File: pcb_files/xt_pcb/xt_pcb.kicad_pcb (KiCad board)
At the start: 2 copper layers, 400.1 x 95.2 mm, 193 parts, among them J1 JST, SW1 RST, SW10 SW_Push, SW11 SW_Push, SW12 SW_Push, SW13 SW_Push, SW14 SW_Push, SW15 SW_Push, SW16 SW_Push, SW17 SW_Push, SW18 SW_Push, SW19 SW_Push, SW2 RST, SW20 SW_Push, SW21 SW_Push, SW22 SW_Push, SW23 SW_Push, SW24 SW_Push, SW25 SW_Push, SW26 SW_Push, SW27 SW_Push, SW28 SW_Push, SW29 SW_Push, SW3 SW_Push, SW30 SW_Push, SW31 SW_Push, SW32 SW_Push, SW33 SW_Push, SW34 SW_Push, SW35 SW_Push, SW36 SW_Push, SW37 SW_Push, SW38 SW_Push, SW39 SW_Push, SW4 SW_Push, SW40 SW_Push, SW41 SW_Push, SW42 SW_Push, SW43 SW_Push, SW44 SW_Push, SW45 SW_Push, SW46 SW_Push, SW47 SW_Push, SW48 SW_Push, SW49 SW_Push, SW5 SW_Push, SW50 SW_Push, SW51 SW_Push, SW52 SW_Push, SW53 SW_Push, SW54 SW_Push, SW55 SW_Push, SW56 SW_Push, SW57 SW_Push, SW58 SW_Push, SW59 SW_Push, SW6 SW_Push, SW60 SW_Push, SW61 SW_Push, SW62 SW_Push, SW63 SW_Push, SW64 SW_Push, SW65 SW_Push, SW66 SW_Push, SW67 SW_Push, SW68 SW_Push, SW69 SW_Push, SW7 SW_Push, SW70 SW_Push, SW71 SW_Push, SW72 SW_Push, SW73 SW_Push, SW74 SW_Push, SW75 SW_Push, SW76 SW_Push, SW77 SW_Push, SW78 SW_Push, SW79 SW_Push, SW8 SW_Push, SW80 SW_Push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

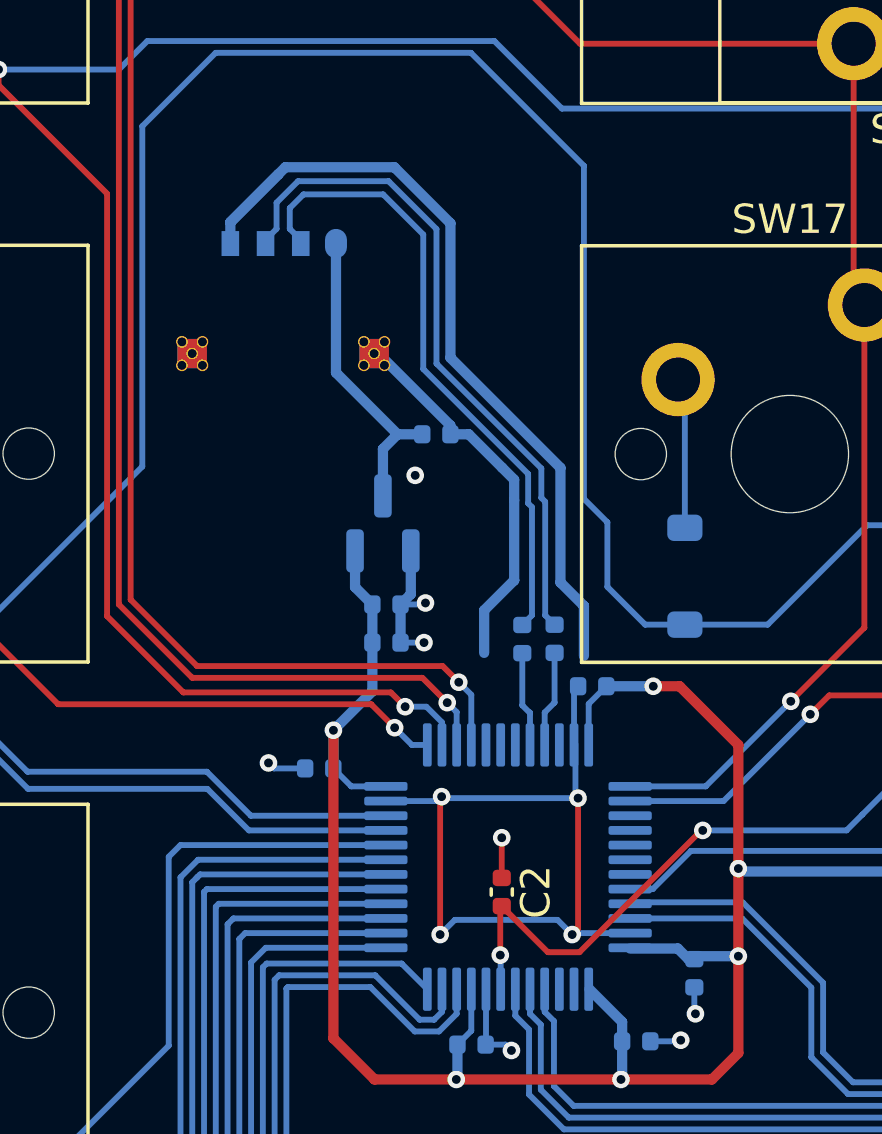
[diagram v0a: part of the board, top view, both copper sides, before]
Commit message: 0603 handsolder
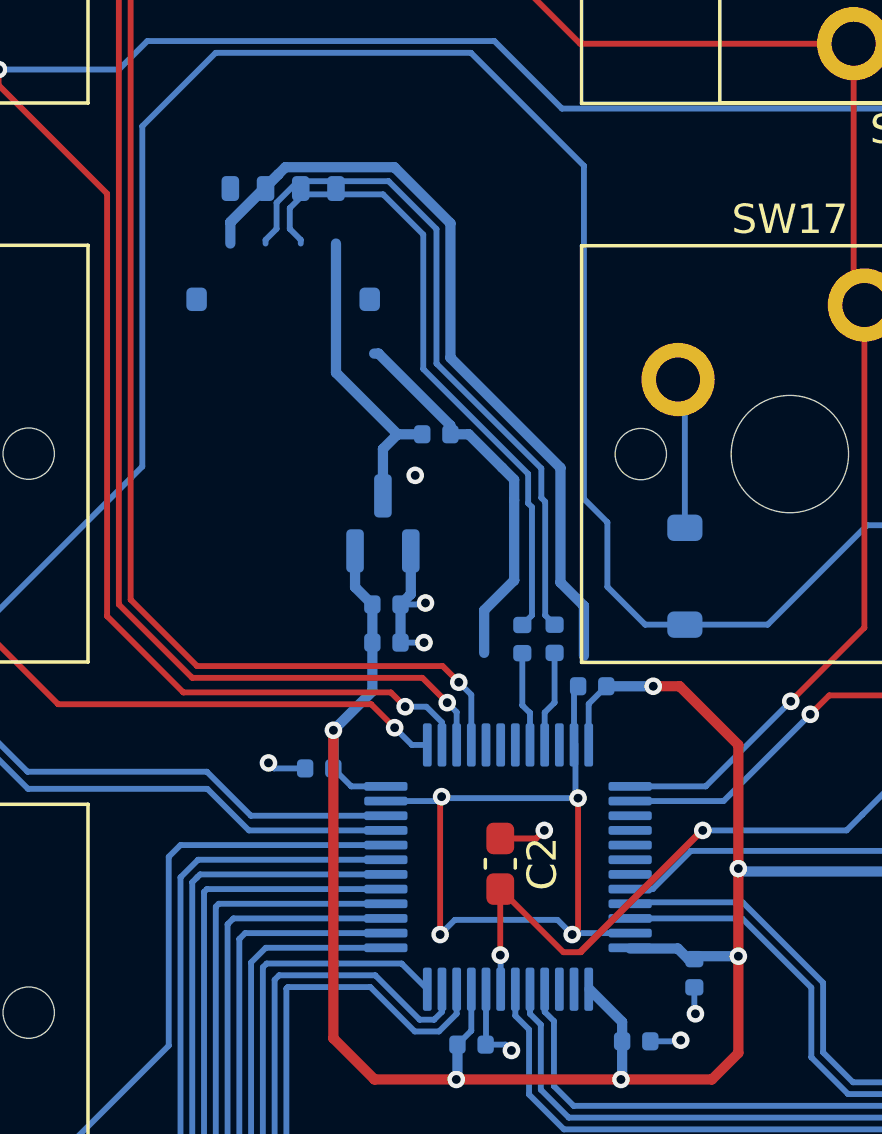
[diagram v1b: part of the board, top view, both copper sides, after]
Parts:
- C2: footprint Capacitor_SMD:C_0402_1005Metric -> Capacitor_SMD:C_0603_1608Metric_Pad1.08x0.95mm_HandSolder
- J1: footprint acheron_Connectors:MOLEX_781710004_MountingReliefs -> Connector_Molex:Molex_Pico-EZmate_78171-0004_1x04-1MP_P1.20mm_Vertical
- SW17: footprint PCM_Switch_Keyboard_Cherry_MX:SW_Cherry_MX_PCB_1.25u -> PCM_Switch_Keyboard_Cherry_MX:SW_Cherry_MX_PCB_2.25u
- SW72: footprint PCM_Switch_Keyboard_Cherry_MX:SW_Cherry_MX_PCB_1.75u -> PCM_Switch_Keyboard_Cherry_MX:SW_Cherry_MX_PCB_2.75u
- moved C2 0.96 mm to (115.7, 161.6)
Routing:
- net Net-(J1-Pin_3): track 23.1 -> 51.9 mm
- net GND: track 90.5 -> 62.0 mm
- net NRST: track 25.9 -> 32.6 mm

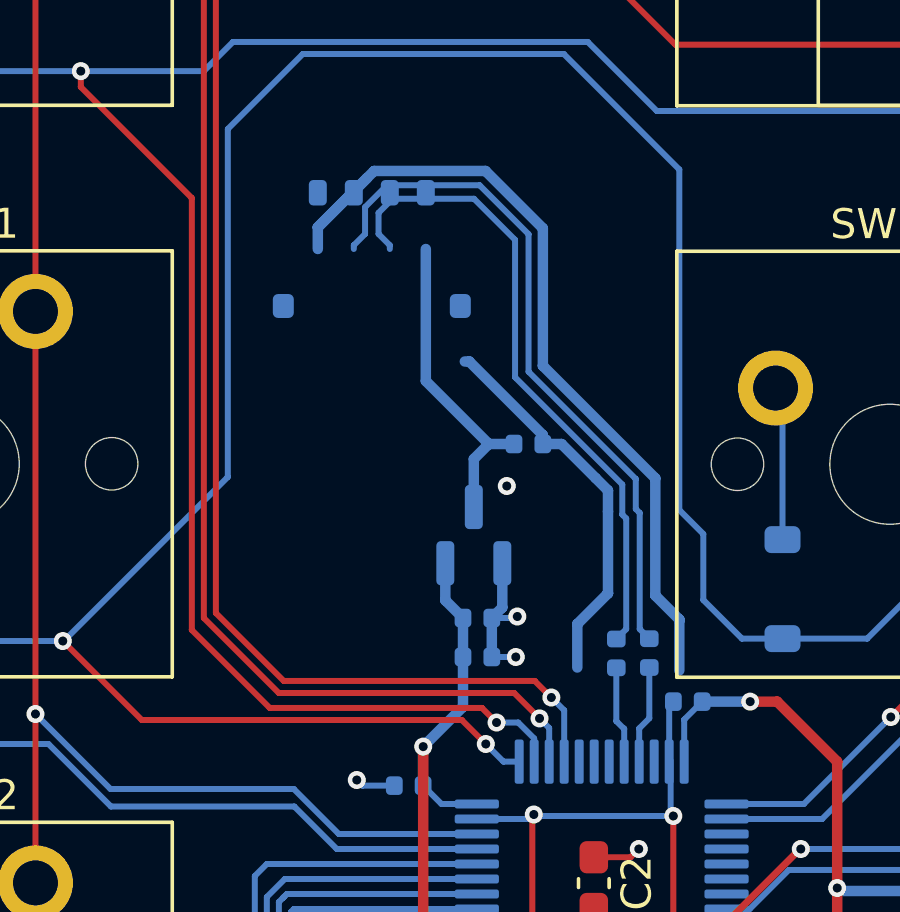
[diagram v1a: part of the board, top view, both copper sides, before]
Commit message: allignment fix
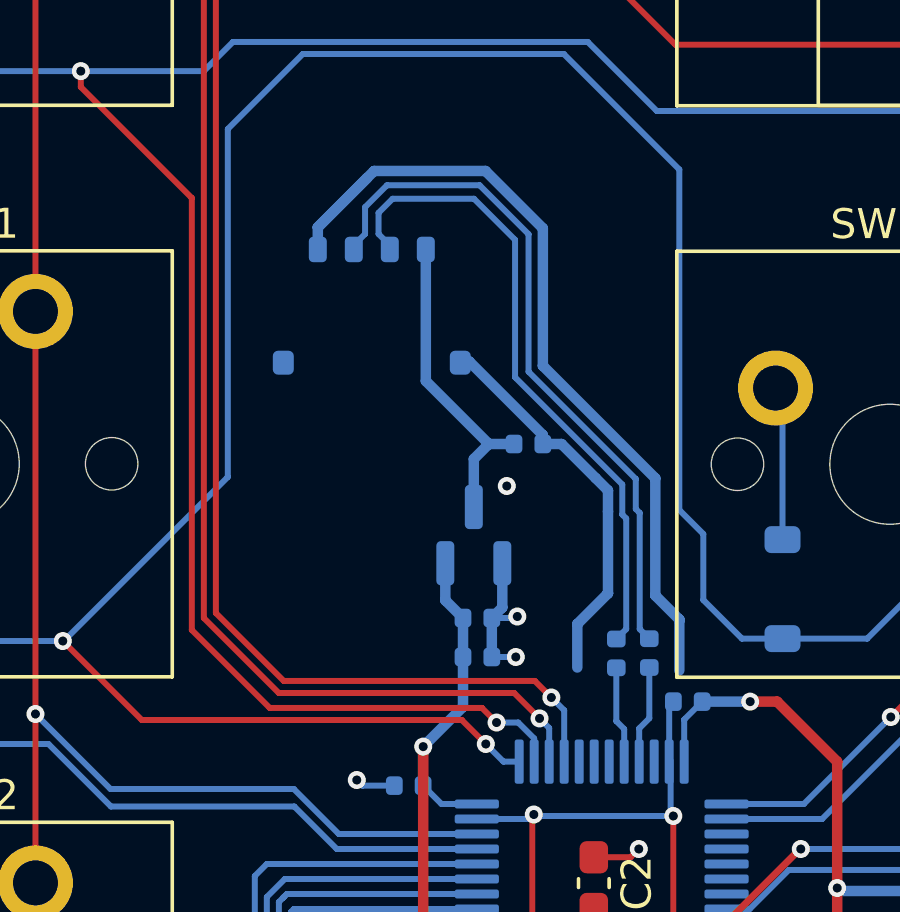
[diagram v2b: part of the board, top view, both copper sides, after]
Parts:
- moved J1 1.89 mm to (108.3, 142.3)
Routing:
- net GND: track 62.0 -> 90.8 mm
- net Net-(J1-Pin_3): track 51.9 -> 23.1 mm
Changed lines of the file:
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@@
 	(footprint "Connector_Molex:Molex_Pico-EZmate_78171-0004_1x04-1MP_P1.20mm_Vertical"
 		(layer "B.Cu")
-		(at 108.2615 140.445 180)
+		(at 108.2615 142.335 180)
 		(descr "Molex Pico-EZmate series connector, 78171-0004 (http://www.molex.com/pdm_docs/sd/781710002_sd.pdf), generated with kicad-footprint-generator")
 		(tags "connector Molex Pico-EZmate vertical")
@@
 	)
 	(segment
-		(start 111.6615 149.045)
-		(end 111.6615 147.445)
+		(start 110.0615 144.845)
+		(end 110.0615 140.46)
 		(width 0.35)
 		(layer "B.Cu")
@@
 	)
 	(segment
-		(start 111.6615 147.445)
-		(end 112.1615 146.945)
+		(start 111.6615 149.045)
+		(end 111.6615 147.445)
 		(width 0.35)
 		(layer "B.Cu")
@@
 	)
 	(segment
-		(start 110.0615 140.445)
-		(end 110.0615 144.845)
+		(start 111.6615 147.445)
+		(end 112.1615 146.945)
 		(width 0.35)
 		(layer "B.Cu")
@@
 	)
 	(segment
+		(start 112.051864 137.844)
+		(end 113.9625 139.754636)
+		(width 0.35)
+		(layer "B.Cu")
+		(net 2)
+	)
+	(segment
 		(start 112.6115 150.92)
 		(end 112.6115 152.395)
@@
 	)
 	(segment
+		(start 106.4615 139.72)
+		(end 108.099 138.0825)
+		(width 0.35)
+		(layer "B.Cu")
+		(net 2)
+	)
+	(segment
+		(start 108.099 138.0825)
+		(end 108.337501 137.844)
+		(width 0.35)
+		(layer "B.Cu")
+		(net 2)
+	)
+	(segment
 		(start 115.174 165.8575)
 		(end 115.174 167.7325)
@@
 	)
 	(segment
+		(start 118.5115 152.795)
+		(end 118.5115 154.495)
+		(width 0.35)
+		(layer "B.Cu")
+		(net 2)
+	)
+	(segment
+		(start 118.5115 152.795)
+		(end 118.5115 152.845)
+		(width 0.35)
+		(layer "B.Cu")
+		(net 2)
+	)
+	(segment
 		(start 113.9615 146.945)
 		(end 114.5865 146.945)
@@
 	)
 	(segment
+		(start 117.7115 148.0873)
+		(end 117.7115 151.995)
+		(width 0.35)
+		(layer "B.Cu")
+		(net 2)
+	)
+	(segment
 		(start 113.6115 163.995)
 		(end 114.1125 163.494)
@@
 	)
 	(segment
+		(start 108.337501 137.844)
+		(end 112.051864 137.844)
+		(width 0.35)
+		(layer "B.Cu")
+		(net 2)
+	)
+	(segment
 		(start 114.1125 163.494)
 		(end 117.6105 163.494)
@@
 	)
 	(segment
+		(start 113.9625 144.3383)
+		(end 117.7115 148.0873)
+		(width 0.35)
+		(layer "B.Cu")
+		(net 2)
+	)
+	(segment
 		(start 122.274 166.6575)
 		(end 122.3115 166.695)
@@
 	)
 	(segment
+		(start 106.4615 139.720001)
+		(end 108.099 138.0825)
+		(width 0.35)
+		(layer "B.Cu")
+		(net 2)
+	)
+	(segment
+		(start 117.7115 151.995)
+		(end 118.5115 152.795)
+		(width 0.35)
+		(layer "B.Cu")
+		(net 2)
+	)
+	(segment
 		(start 113.0615 152.745)
 		(end 113.1115 152.695)
@@
 	)
 	(segment
+		(start 106.4615 140.445)
+		(end 106.4615 139.72)
+		(width 0.35)
+		(layer "B.Cu")
+		(net 2)
+	)
+	(segment
 		(start 112.2615 154.045)
 		(end 113.0615 154.045)
@@
 	)
 	(segment
+		(start 113.9625 139.754636)
+		(end 113.9625 144.3383)
+		(width 0.35)
+		(layer "B.Cu")
+		(net 2)
+	)
+	(segment
 		(start 434.6815 111.795)
 		(end 434.6815 108.0465)
@@
 	)
 	(segment
-		(start 116.674 156.426249)
-		(end 116.674 156.445)
-		(width 0.2)
-		(layer "B.Cu")
-		(net 116)
-	)
-	(segment
 		(start 116.674 156.445)
 		(end 116.4115 156.1825)
@@
 	)
 	(segment
-		(start 112.051864 137.844)
-		(end 113.9625 139.754636)
-		(width 0.35)
-		(layer "B.Cu")
-		(net 129)
-	)
-	(segment
 		(start 108.0365 139.945)
 		(end 107.6615 140.32)
@@
 	)
 	(segment
-		(start 106.4615 139.72)
-		(end 108.099 138.0825)
-		(width 0.35)
-		(layer "B.Cu")
-		(net 129)
-	)
-	(segment
 		(start 108.0365 139.051802)
 		(end 108.0365 139.945)
@@
 	)
 	(segment
-		(start 108.099 138.0825)
-		(end 108.337501 137.844)
-		(width 0.35)
-		(layer "B.Cu")
-		(net 129)
-	)
-	(segment
-		(start 118.5115 152.795)
-		(end 118.5115 154.495)
-		(width 0.35)
-		(layer "B.Cu")
-		(net 129)
-	)
-	(segment
-		(start 118.5115 152.795)
-		(end 118.5115 152.845)
-		(width 0.35)
-		(layer "B.Cu")
-		(net 129)
-	)
-	(segment
 		(start 117.191501 153.115001)
 		(end 117.191501 149.242101)
@@
 	)
 	(segment
-		(start 117.7115 148.0873)
-		(end 117.7115 151.995)
-		(width 0.35)
-		(layer "B.Cu")
-		(net 129)
-	)
-	(segment
-		(start 108.337501 137.844)
-		(end 112.051864 137.844)
-		(width 0.35)
-		(layer "B.Cu")
-		(net 129)
-	)
-	(segment
 		(start 113.4865 139.951802)
 		(end 111.854698 138.32)
@@
 	)
 	(segment
-		(start 113.9625 144.3383)
-		(end 117.7115 148.0873)
-		(width 0.35)
-		(layer "B.Cu")
-		(net 129)
-	)
-	(segment
 		(start 117.0605 148.109466)
 		(end 113.4865 144.535466)
@@
 	)
 	(segment
-		(start 106.4615 139.720001)
-		(end 108.099 138.0825)
-		(width 0.35)
-		(layer "B.Cu")
-		(net 129)
-	)
-	(segment
-		(start 117.7115 151.995)
-		(end 118.5115 152.795)
-		(width 0.35)
-		(layer "B.Cu")
-		(net 129)
-	)
-	(segment
 		(start 108.768302 138.32)
 		(end 108.0365 139.051802)
@@
 		(layer "B.Cu")
 		(net 129)
-	)
-	(segment
-		(start 106.4615 140.445)
-		(end 106.4615 139.72)
-		(width 0.35)
-		(layer "B.Cu")
-		(net 129)
-	)
-	(segment
-		(start 113.9625 139.754636)
-		(end 113.9625 144.3383)
-		(width 0.35)
-		(layer "B.Cu")
-		(net 129)

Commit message: new footprint
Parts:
- SW17: footprint PCM_Switch_Keyboard_Cherry_MX:SW_Cherry_MX_PCB_2.25u -> PCM_Switch_Keyboard_Cherry_MX:SW_Cherry_MX_PCB_1.25u
- SW72: footprint PCM_Switch_Keyboard_Cherry_MX:SW_Cherry_MX_PCB_2.75u -> PCM_Switch_Keyboard_Cherry_MX:SW_Cherry_MX_Plate_1.75u
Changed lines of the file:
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@@
 		)
 	)
-	(footprint "PCM_Switch_Keyboard_Cherry_MX:SW_Cherry_MX_PCB_2.75u"
+	(footprint "PCM_Switch_Keyboard_Cherry_MX:SW_Cherry_MX_Plate_1.75u"
 		(layer "F.Cu")
 		(at 363.60625 147.605)
-		(descr "Cherry MX keyswitch PCB Mount Keycap 2.75u")
-		(tags "Cherry MX Keyboard Keyswitch Switch PCB Cutout Keycap 2.75u")
+		(descr "Cherry MX keyswitch Plate Mount Keycap 1.75u")
+		(tags "Cherry MX Keyboard Keyswitch Switch Plate Cutout Keycap 1.75u")
 		(property "Reference" "SW72"
 			(at 0 -8 0)
@@
 		)
 		(fp_line
-			(start -26.19375 -9.525)
-			(end -26.19375 9.525)
+			(start -16.66875 -9.525)
+			(end -16.66875 9.525)
 			(stroke
 				(width 0.1)
@@
 		)
 		(fp_line
-			(start -26.19375 9.525)
-			(end 26.19375 9.525)
+			(start -16.66875 9.525)
+			(end 16.66875 9.525)
 			(stroke
 				(width 0.1)
@@
 		)
 		(fp_line
-			(start 26.19375 -9.525)
-			(end -26.19375 -9.525)
+			(start 16.66875 -9.525)
+			(end -16.66875 -9.525)
 			(stroke
 				(width 0.1)
@@
 		)
 		(fp_line
-			(start 26.19375 9.525)
-			(end 26.19375 -9.525)
+			(start 16.66875 9.525)
+			(end 16.66875 -9.525)
 			(stroke
 				(width 0.1)
@@
 		)
 		(pad "" np_thru_hole circle
-			(at -5.08 0)
-			(size 1.75 1.75)
-			(drill 1.75)
-			(layers "*.Cu" "*.Mask")
-		)
-		(pad "" np_thru_hole circle
 			(at 0 0)
 			(size 4 4)
@@
 			(layers "*.Cu" "*.Mask")
 		)
-		(pad "" np_thru_hole circle
-			(at 5.08 0)
-			(size 1.75 1.75)
-			(drill 1.75)
-			(layers "*.Cu" "*.Mask")
-		)
 		(pad "1" thru_hole circle
 			(at -3.81 -2.54)
@@
 		)
 		(embedded_fonts no)
-		(model "${KICAD6_3RD_PARTY}/3dmodels/com_github_perigoso_keyswitch-kicad-library/3d-library.3dshapes/SW_Cherry_MX_PCB.wrl"
+		(model "${KICAD6_3RD_PARTY}/3dmodels/com_github_perigoso_keyswitch-kicad-library/3d-library.3dshapes/SW_Cherry_MX_Plate.wrl"
 			(offset
 				(xyz 0 0 0)
@@
 		)
 	)
-	(footprint "PCM_Switch_Keyboard_Cherry_MX:SW_Cherry_MX_PCB_2.25u"
+	(footprint "PCM_Switch_Keyboard_Cherry_MX:SW_Cherry_MX_PCB_1.25u"
 		(layer "F.Cu")
 		(at 125.53 147.62)
-		(descr "Cherry MX keyswitch PCB Mount Keycap 2.25u")
-		(tags "Cherry MX Keyboard Keyswitch Switch PCB Cutout Keycap 2.25u")
+		(descr "Cherry MX keyswitch PCB Mount Keycap 1.25u")
+		(tags "Cherry MX Keyboard Keyswitch Switch PCB Cutout Keycap 1.25u")
 		(property "Reference" "SW17"
 			(at 0 -8 0)
@@
 		)
 		(fp_line
-			(start -21.43125 -9.525)
-			(end -21.43125 9.525)
+			(start -11.90625 -9.525)
+			(end -11.90625 9.525)
 			(stroke
 				(width 0.1)
@@
 		)
 		(fp_line
-			(start -21.43125 9.525)
-			(end 21.43125 9.525)
+			(start -11.90625 9.525)
+			(end 11.90625 9.525)
 			(stroke
 				(width 0.1)
@@
 		)
 		(fp_line
-			(start 21.43125 -9.525)
-			(end -21.43125 -9.525)
+			(start 11.90625 -9.525)
+			(end -11.90625 -9.525)
 			(stroke
 				(width 0.1)
@@
 		)
 		(fp_line
-			(start 21.43125 9.525)
-			(end 21.43125 -9.525)
+			(start 11.90625 9.525)
+			(end 11.90625 -9.525)
 			(stroke
 				(width 0.1)
